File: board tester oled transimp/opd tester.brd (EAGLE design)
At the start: 160 x 100 mm, 18 parts, among them IC1 TL7660, J1 i2c, U1 MCP4725A0T-E/CH, U2 LMC6482AIM/NOPB

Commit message: more work
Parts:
- removed TP2: TEST_POINTTHRU, scono:TEST_POINT
- added R4, R5: 10k, scono:0603-RES
- moved J3 52.3 mm to (15.5, 25.5), turned to 270 degrees
- moved C3 47.9 mm to (13.0, 25.5), turned to 90 degrees
- moved J1 41.0 mm to (15.5, 17.2), turned to 90 degrees
- moved J2 40.2 mm to (3.50, 5.25)
- moved R3 38.5 mm to (11.0, 25.5), turned to 90 degrees
- moved TP1 37.2 mm to (13.5, 8.00)
- moved C1 36.9 mm to (-1.50, 9.50)
- moved U1 36.4 mm to (8.00, 16.2)
- moved IC1 36.1 mm to (2.00, 10.0), turned to 270 degrees
- moved U2 35.0 mm to (5.50, 24.5)
- moved C2 32.5 mm to (10.2, 9.50)
- moved TP5 31.4 mm to (0.25, 22.2)
- moved TP3 30.1 mm to (8.25, 29.0)
- moved R2 27.1 mm to (5.25, 29.2), turned to 180 degrees
- moved TP4 26.4 mm to (0.75, 29.2)
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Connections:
- net 5V: now also R4.2, R5.1
- net OUTSIG: no longer TP2.1
- net SCL: now also R4.1
- net SDA: now also R5.2
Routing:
- net -5V: track 0.00 -> 27.9 mm, vias 0 -> 2
- net GND: track 0.00 -> 12.8 mm, vias 0 -> 6
- net N$3: track 0.00 -> 12.7 mm
- net N$5: track 0.00 -> 12.3 mm
- net SCL: track 0.00 -> 10.2 mm
- net SDA: track 0.00 -> 9.69 mm
- net N$4: track 0.00 -> 9.54 mm
- net OUTSIG: track 0.00 -> 8.97 mm
- net N$1: track 0.00 -> 4.54 mm
- net N$2: track 0.00 -> 4.00 mm
- net OPD_BIAS: track 0.00 -> 3.37 mm
- added copper zone on layer 1, net 5V
- added copper zone on layer 16, net GND
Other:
- board size 160 x 100 mm -> 21 x 27.5 mm

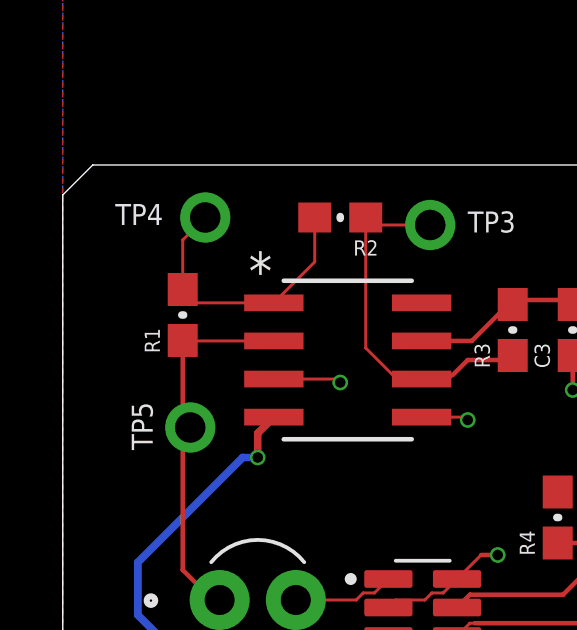
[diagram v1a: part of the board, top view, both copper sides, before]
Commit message: add cap for stabalization
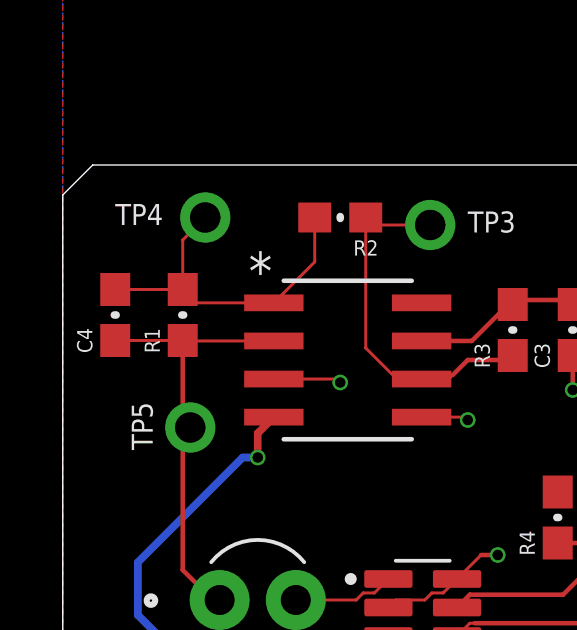
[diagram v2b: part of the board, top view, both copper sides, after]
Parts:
- added C4: 0.1uF, scono:0603-CAP
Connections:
- net N$3: now also C4.1
- net N$4: now also C4.2
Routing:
- net N$3: track 12.7 -> 15.0 mm
- net N$4: track 9.54 -> 11.8 mm
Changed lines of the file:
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@@
 <attribute name="VALUE" x="14.397" y="12.73" size="0.508" layer="27" font="vector" rot="R90"/>
+</element>
+<element name="C4" library="scono" library_urn="urn:adsk.eagle:library:14850048" package="0603-CAP" package3d_urn="urn:adsk.eagle:package:14850677/1" value="0.1uF" x="-2.25" y="26" smashed="yes" rot="R90">
+<attribute name="NAME" x="-3.012" y="24.73" size="0.508" layer="25" font="vector" ratio="10" rot="R90"/>
+<attribute name="PIE-INT-REF-NUM" value="CAPACITOR-GENERIC" x="-2.25" y="26" size="1.778" layer="27" rot="R90" display="off"/>
+<attribute name="VALUE" x="-0.853" y="24.73" size="0.508" layer="27" font="vector" rot="R90"/>
 </element>
 </elements>
@@
 <wire x1="0" y1="25.15" x2="0.015" y2="25.135" width="0.1" layer="1"/>
 <wire x1="0.015" y1="25.135" x2="3.0362" y2="25.135" width="0.1" layer="1"/>
+<contactref element="C4" pad="1"/>
+<wire x1="-2.25" y1="25.15" x2="-0.15" y2="25.15" width="0.1" layer="1"/>
+<wire x1="-0.15" y1="25.15" x2="0" y2="25" width="0.1" layer="1"/>
 </signal>
 <signal name="N$4">
@@
 <wire x1="3.0362" y1="26.405" x2="4.4" y2="27.7688" width="0.1" layer="1"/>
 <wire x1="4.4" y1="27.7688" x2="4.4" y2="29.25" width="0.1" layer="1"/>
+<contactref element="C4" pad="2"/>
+<wire x1="0" y1="26.85" x2="-2.25" y2="26.85" width="0.1" layer="1"/>
 </signal>
 <signal name="N$5">
